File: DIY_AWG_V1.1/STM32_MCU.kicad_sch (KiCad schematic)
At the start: 25 parts, among them J1 Conn_01x04_Pin, J2 USB_C_Receptacle_USB2.0_16P, J5 Conn_01x12, SW1 SW_Push, SW2 SW_Push, U4 AMS1117-3.3, U7 STM32G473VETx, U8 USBLC6-2SC6, Y1 O925208MEDA4SI

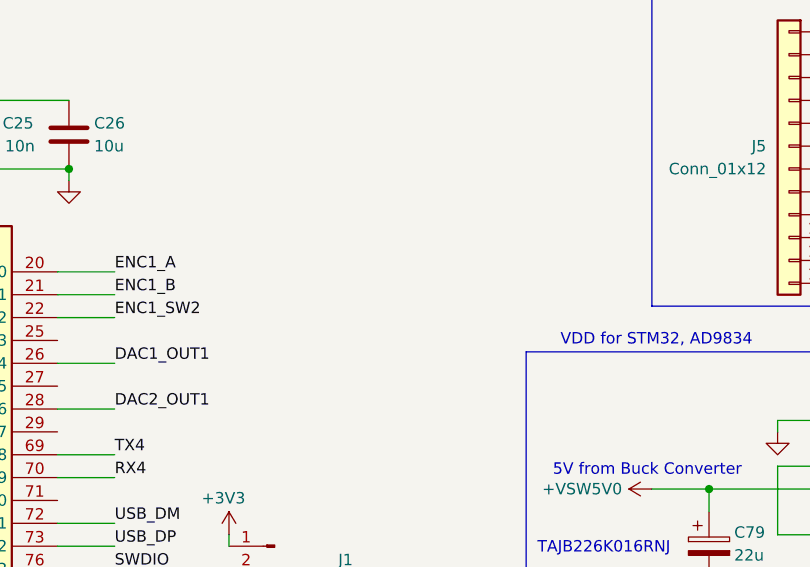
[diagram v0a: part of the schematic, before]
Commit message: Updated AD9834_DDS, STM32_MCU, amplifier schematic
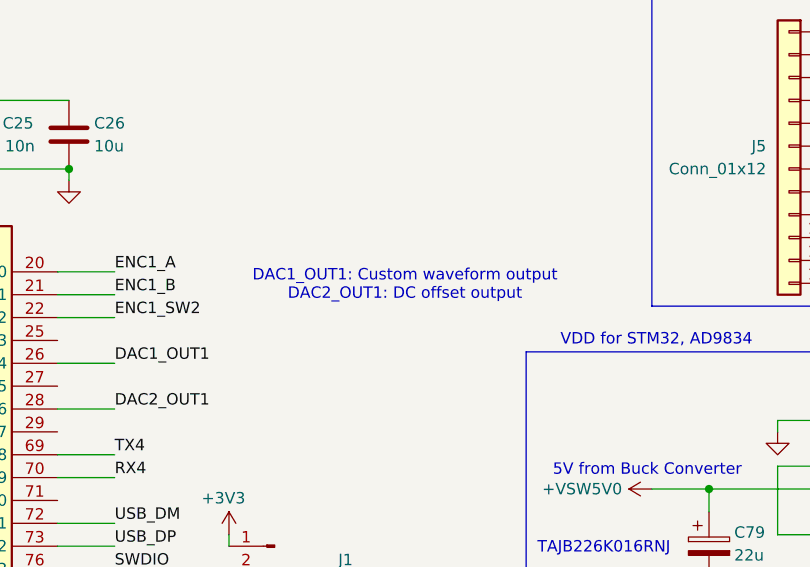
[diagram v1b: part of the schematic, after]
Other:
- note added: "DAC1_OUT1: Custom waveform output DAC2_OUT1: DC offset output"
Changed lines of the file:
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@@
+		)
+	)
+	(text "DAC1_OUT1: Custom waveform output\nDAC2_OUT1: DC offset output"
+		(exclude_from_sim no)
+		(at 193.548 48.514 0)
+		(effects
+			(font
+				(size 1.27 1.27)
+			)
 		)
 	)

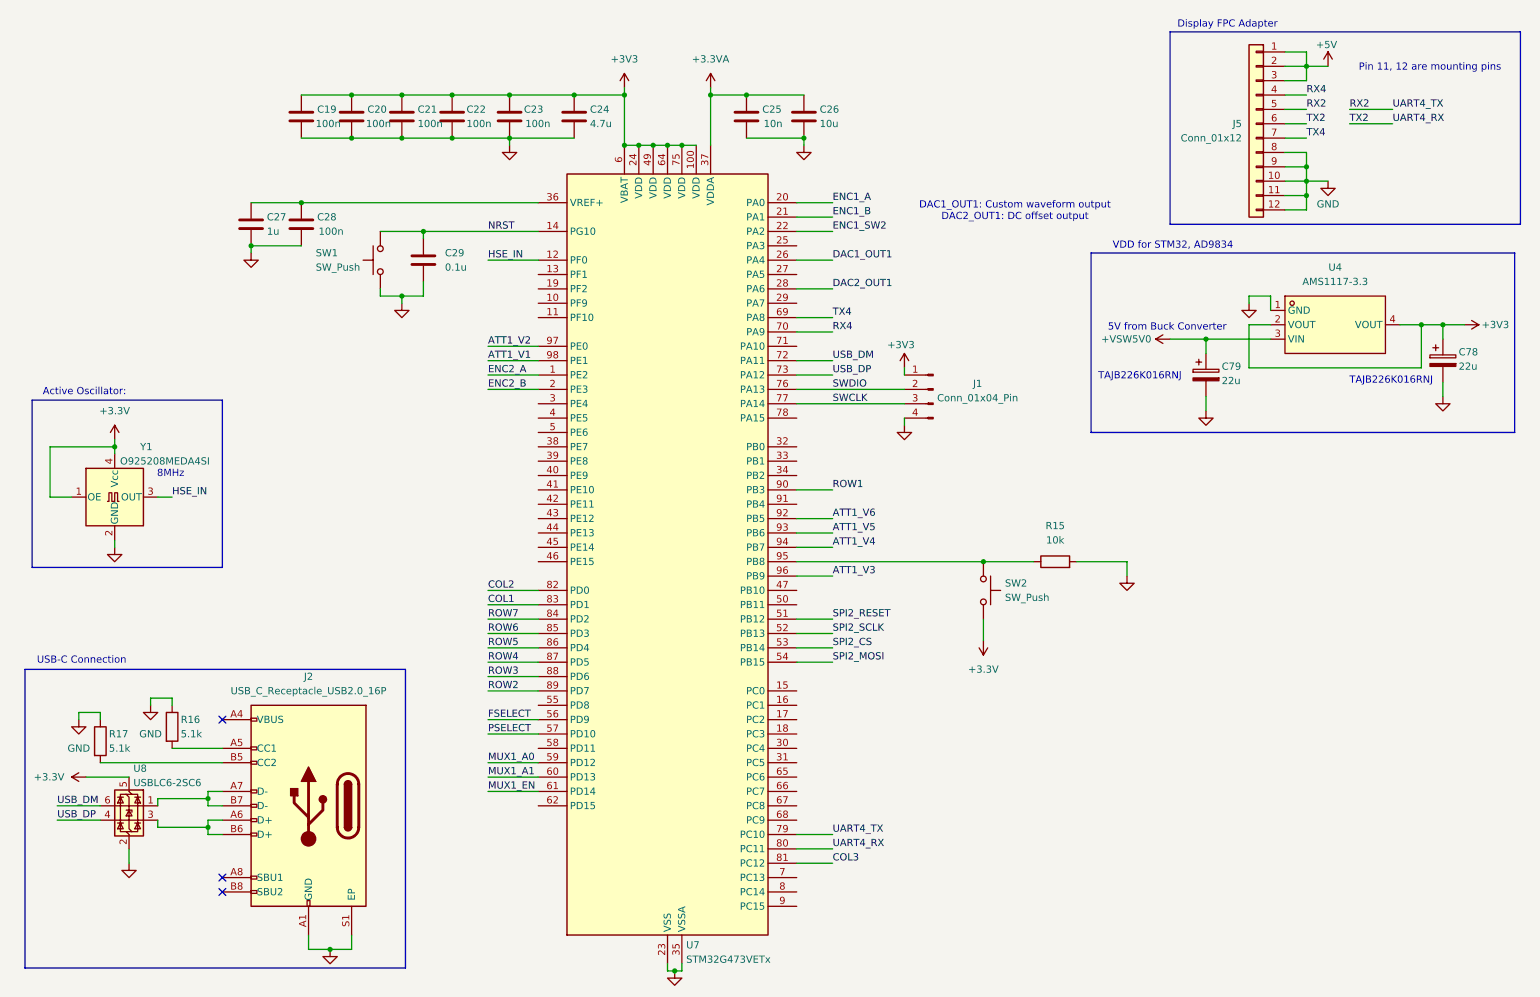
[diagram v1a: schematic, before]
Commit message: Updated AD9834_DDS, amplifier, STM32_MCU schematic
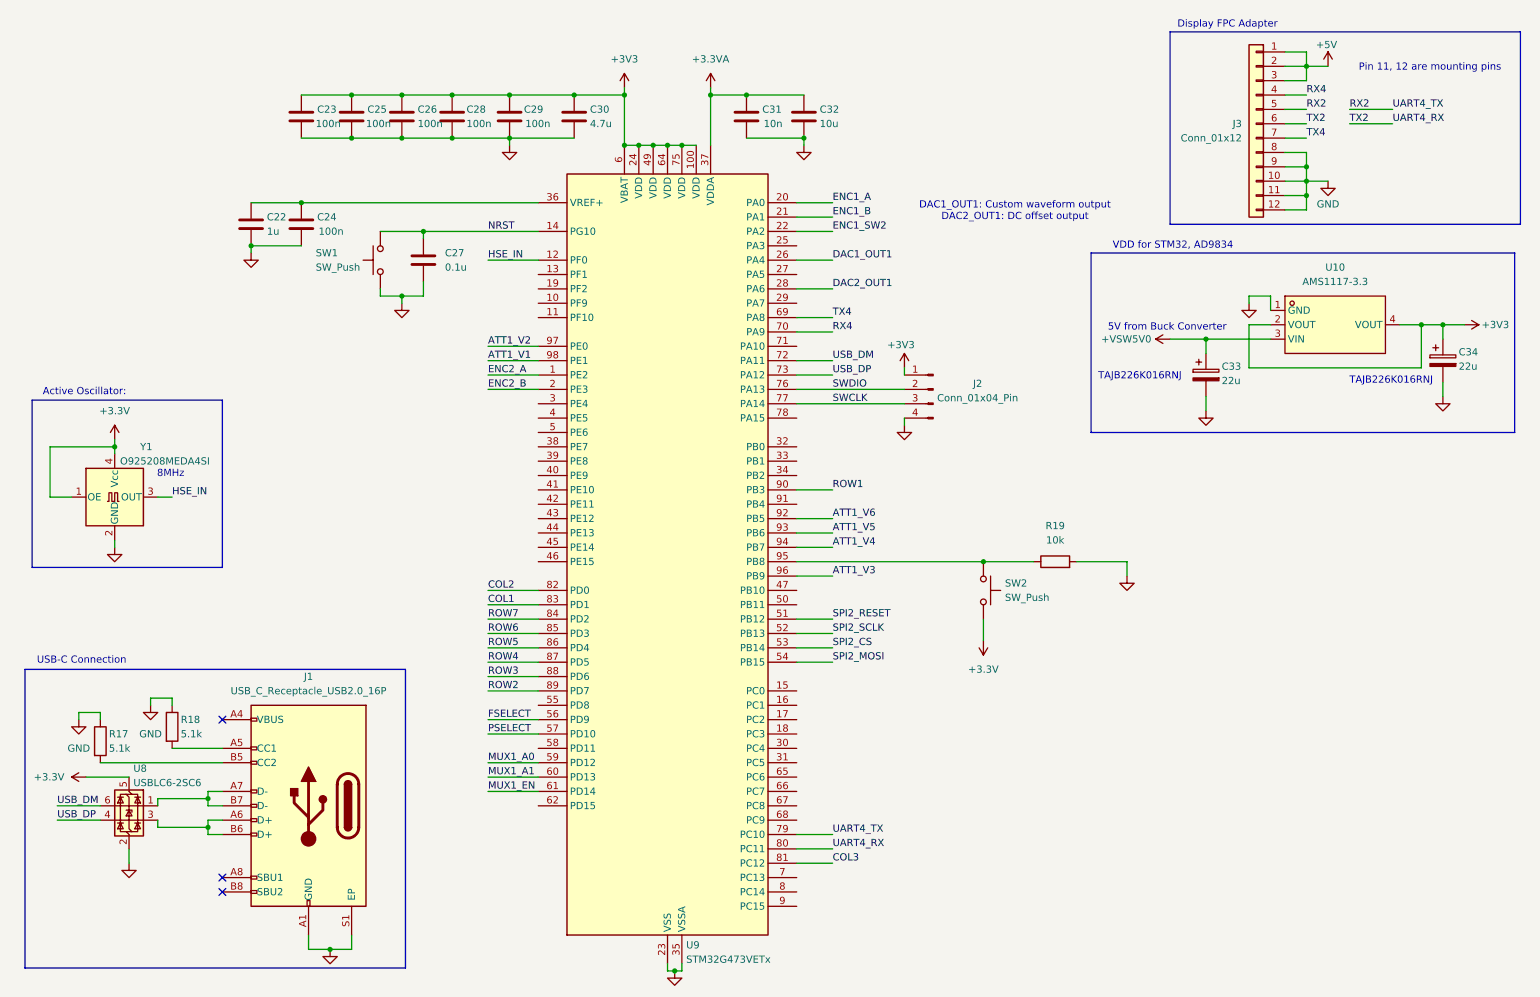
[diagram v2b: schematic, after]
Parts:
- renumbered C27 to C22, C19 to C23, C28 to C24, C20 to C25, C21 to C26, C29 to C27, C22 to C28, C23 to C29, C24 to C30, C25 to C31, C26 to C32, C79 to C33, C78 to C34, J2 to J1, J1 to J2, J5 to J3, R16 to R18, R15 to R19, U4 to U10, U7 to U9

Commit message: Updated STM32_MCU schematic
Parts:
- removed C33, C34: 22u, symbol Device:C_Polarized
- removed U10: AMS1117-3.3, easyeda2kicad:SOT-223-3_L6.5-W3.4-P2.30-LS7.0-BR, symbol easyeda2kicad:AMS1117-3.3
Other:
- note removed: "5V from Buck Converter"
- note removed: "TAJB226K016RNJ"
- note removed: "VDD for STM32, AD9834"

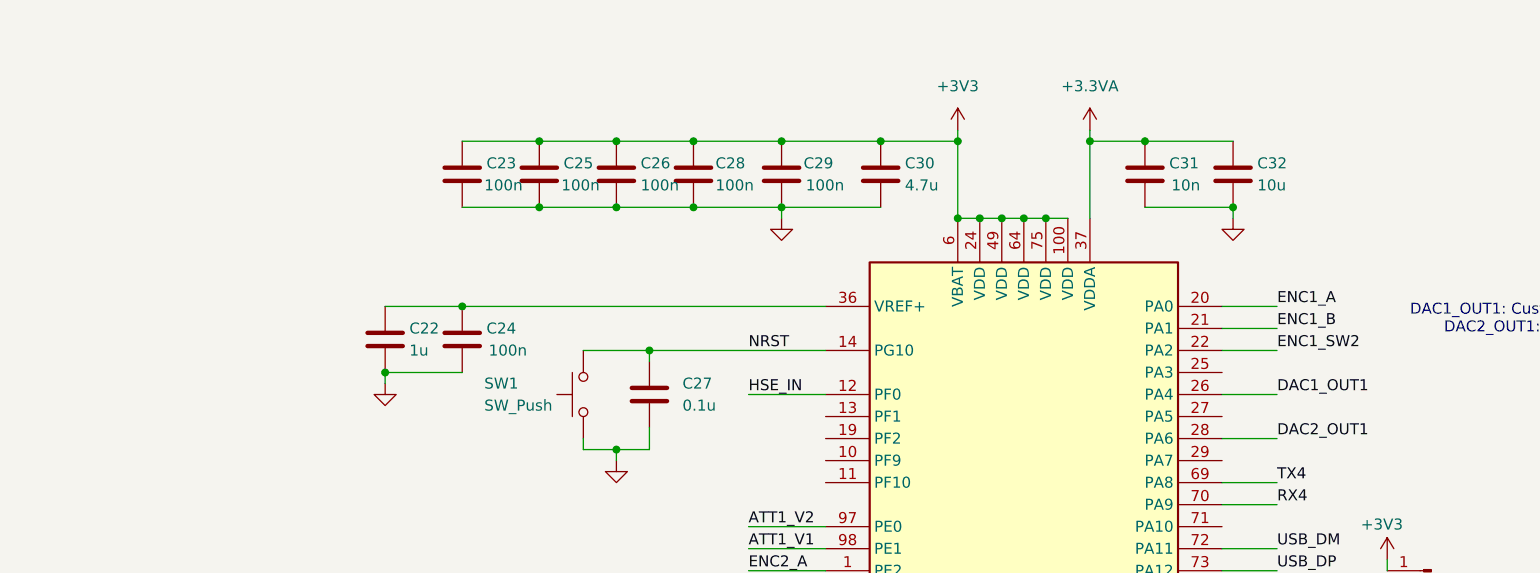
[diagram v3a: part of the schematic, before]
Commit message: Updated amplifier, STM32_MCU schematic
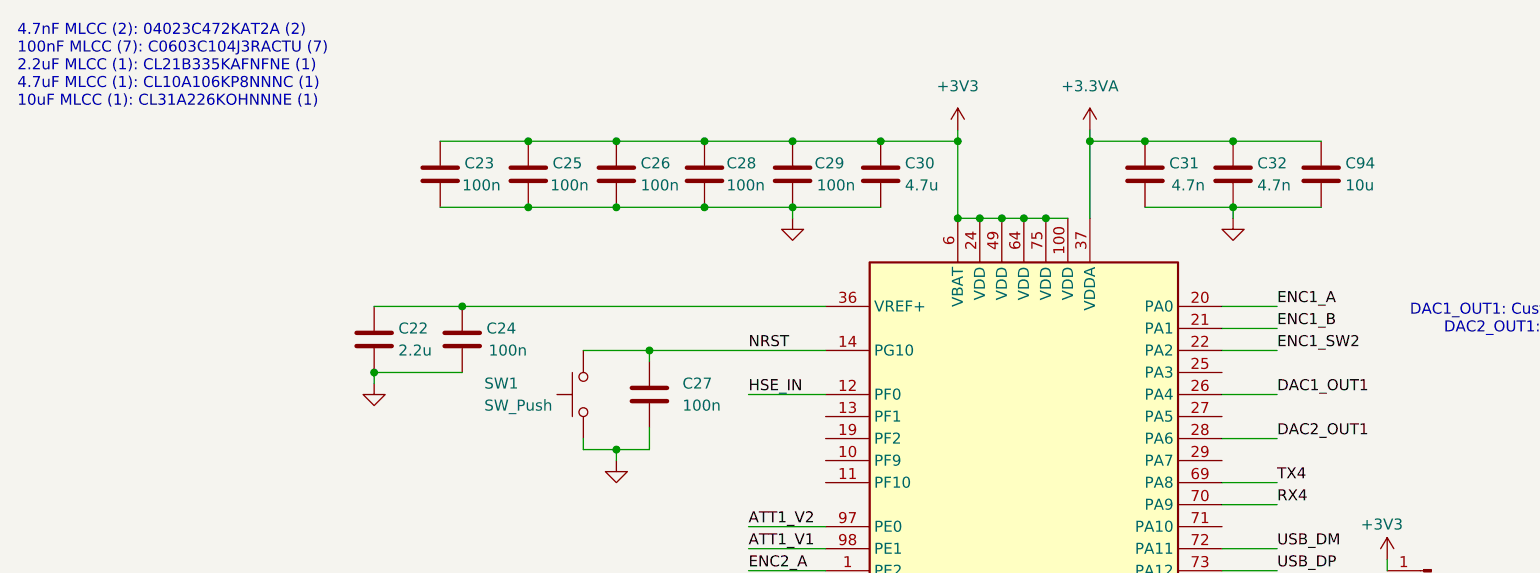
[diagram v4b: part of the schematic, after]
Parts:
- added C94: 10u, symbol Device:C
- C22: value 1u -> 2.2u
- C27: value 0.1u -> 100n
- C31: value 10n -> 4.7n
- C32: value 10u -> 4.7n
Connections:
- net +3.3VA: now also C94.1
- net GND: now also C94.2
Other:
- note added: "4.7nF MLCC (2): 04023C472KAT2A (2) 100nF MLCC (7): C0603C104J3RACTU (7) 2.2uF MLCC (1): CL21B335KAFNFNE (1) 4.7uF MLCC (1): CL10A106KP8NNNC (1) 10uF MLCC (1): CL31A226KOHNNNE (1)"
- moved on the sheet: C22, C23, C25, C28, C29

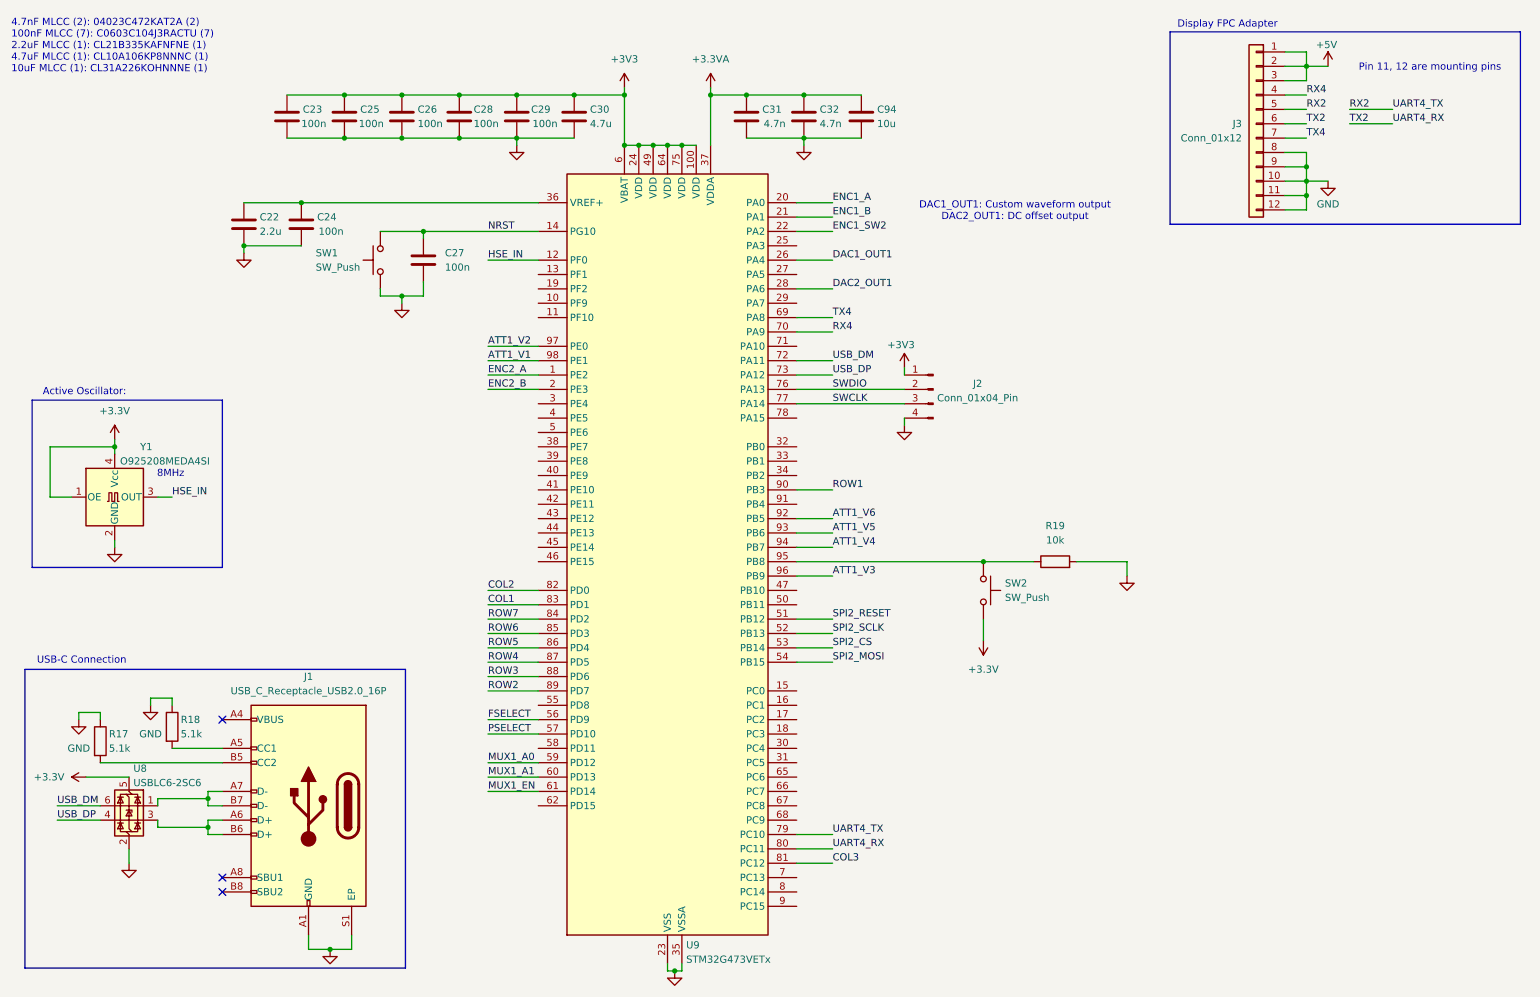
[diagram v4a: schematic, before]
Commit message: Updated STM32_MCU, amplifier schematic
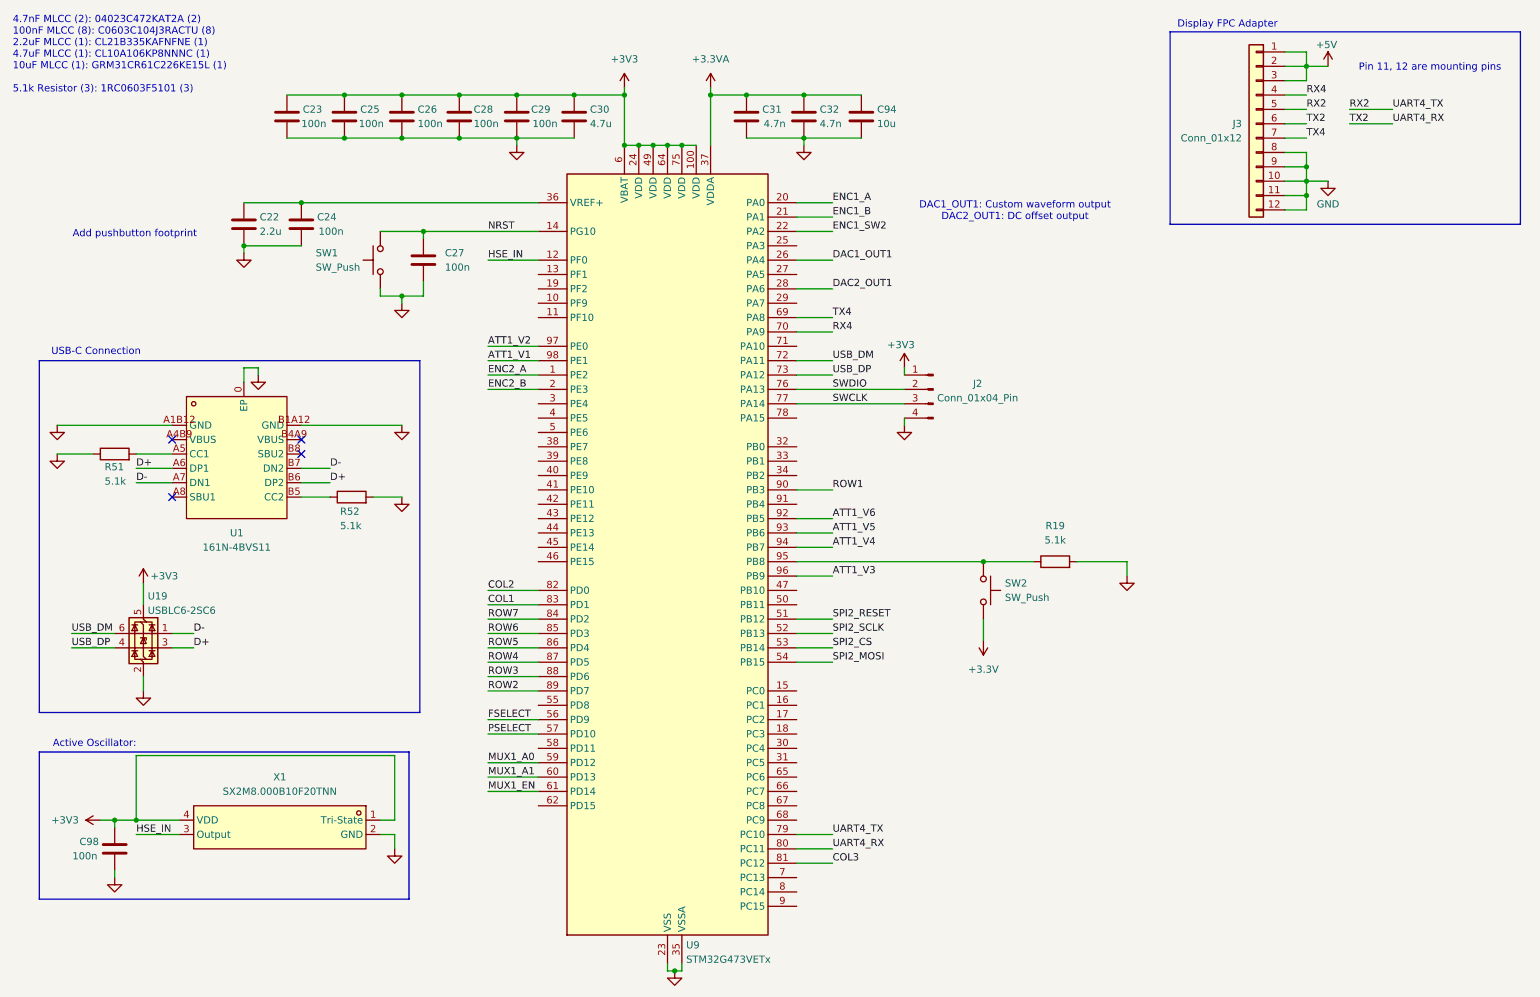
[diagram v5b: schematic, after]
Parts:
- removed J1: USB_C_Receptacle_USB2.0_16P, symbol Connector:USB_C_Receptacle_USB2.0_16P
- removed R17, R18: 5.1k, symbol Device:R
- removed U8: USBLC6-2SC6, Package_TO_SOT_SMD:SOT-23-6, symbol Power_Protection:USBLC6-2SC6
- removed Y1: O925208MEDA4SI, Oscillator:Oscillator_SMD_SeikoEpson_SG8002JA-4Pin_14.0x8.7mm, symbol Oscillator:SG-615
- added C98: 100n, symbol Device:C
- added R51, R52: 5.1k, symbol Device:R
- added U1: 161N-4BVS11, easyeda2kicad:USB-C-SMD_HANELECTRICITY_161N-4XVS11, symbol easyeda2kicad:161N-4BVS11
- added U19: USBLC6-2SC6, Package_TO_SOT_SMD:SOT-23-6, symbol Power_Protection:USBLC6-2SC6
- added X1: SX2M8.000B10F20TNN, easyeda2kicad:OSC-SMD_4P-L2.5-W2.0-BL, symbol easyeda2kicad:SX2M8.000B10F20TNN
- R19: value 10k -> 5.1k
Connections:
- net +3V3: now also C98.1, U19.5 (VBUS), X1.1 (Tri-State), X1.4 (VDD)
- net GND: now also C98.2, R51.1, R52.2, U1.0 (EP), U1.A1B12 (GND), U1.B1A12 (GND), U19.2 (GND), X1.2 (GND)
- net HSE_IN: now also X1.3 (Output)
- net USB_DM: now also U19.6 (I/O1)
- net USB_DP: now also U19.4 (I/O2)
- new net: R52.1, U1.B5 (CC2)
- new net: R51.2, U1.A5 (CC1)
- new net D+: U1.A6 (DP1), U1.B6 (DP2), U19.3 (I/O2)
- new net D-: U1.A7 (DN1), U1.B7 (DN2), U19.1 (I/O1)
- no-connect marks 3 -> 4
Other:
- note added: "4.7nF MLCC (2): 04023C472KAT2A (2) 100nF MLCC (8): C0603C104J3RACTU (8) 2.2uF MLCC (1): CL21B335KAFNFNE (1) 4.7uF MLCC (1): CL10A106KP8NNNC (1) 10uF MLCC (1): GRM31CR61C226KE15L (1) 5.1k Resistor (3): 1RC0603F5101 (3)"
- note added: "Add pushbutton footprint"
- note removed: "4.7nF MLCC (2): 04023C472KAT2A (2) 100nF MLCC (7): C0603C104J3RACTU (7) 2.2uF MLCC (1): CL21B335KAFNFNE (1) 4.7uF MLCC (1): CL10A106KP8NNNC (1) 10uF MLCC (1): CL31A226KOHNNNE (1)"
- note removed: "8MHz"
